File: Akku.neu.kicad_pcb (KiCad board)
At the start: 2 copper layers, 100 x 160 mm, 46 parts, among them P1 CONN_02X10, P2 CONN_02X10, P3 CONN_02X10, P4 CONN_01X01, P5 CONN_01X01, P6 CONN_01X01, SW1 SWITCH_INV, SW2 SWITCH_INV, SW3 SWITCH_INV, U1 7400, U2 7408, U3 4069, U4 74LS193, U5 74LS541, U6 74LS193, U7 74LS540, U8 74HC14

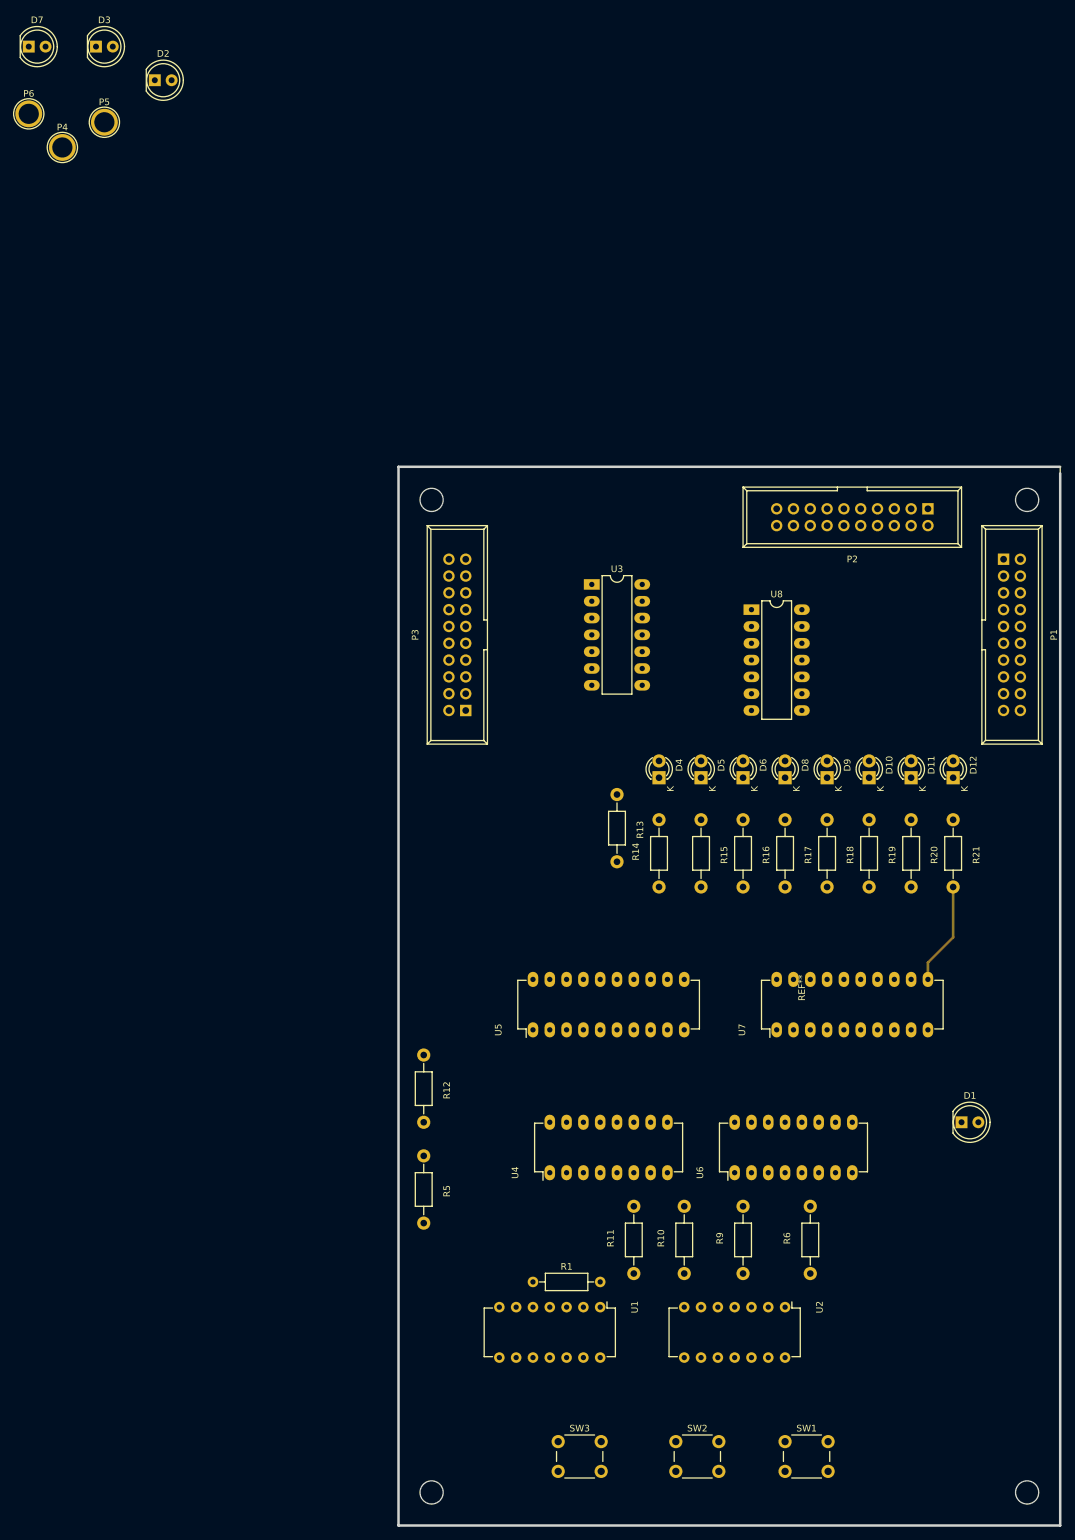
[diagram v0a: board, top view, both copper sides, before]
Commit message: Akku.sch fertiggestellt, Footprintfehler behoben, PCB Grundauslegung begonnen
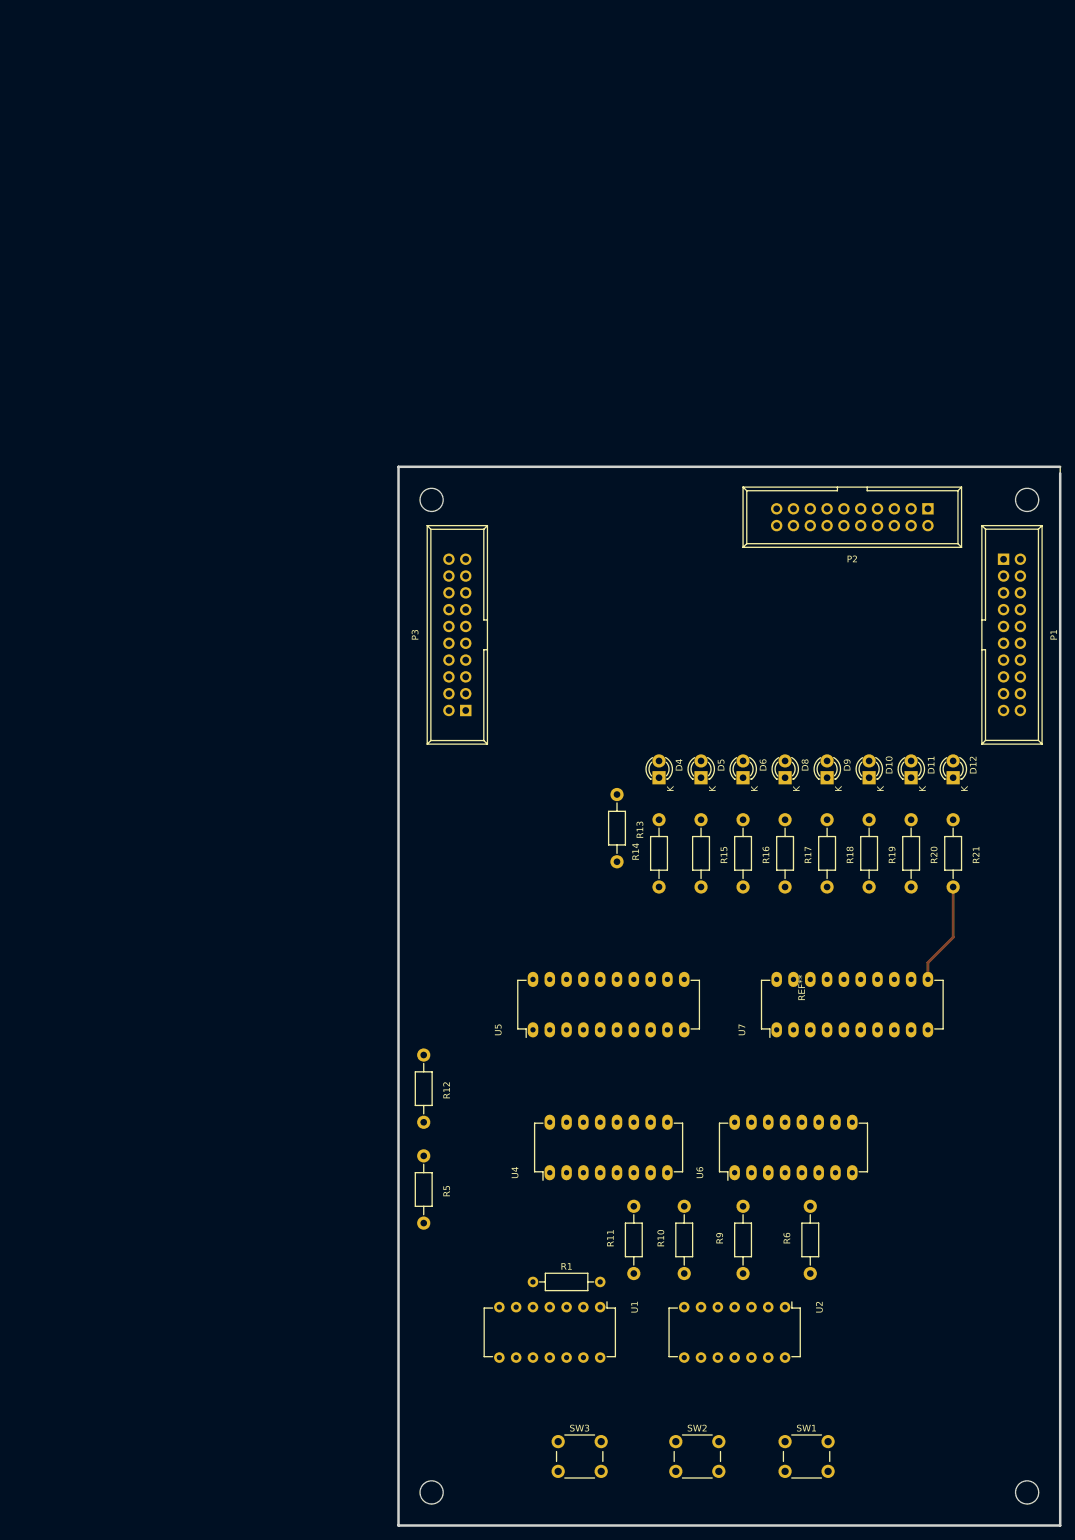
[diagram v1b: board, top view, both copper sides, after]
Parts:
- removed D1, D2, D3, D7: LED, LEDs:LED_D5.0mm_FlatTop
- removed P4, P5, P6: CONN_01X01, Connect:1pin
- removed U3: 4069, Housings_DIP:DIP-14_W7.62mm_LongPads
- removed U8: 74HC14, Housings_DIP:DIP-14_W7.62mm_LongPads

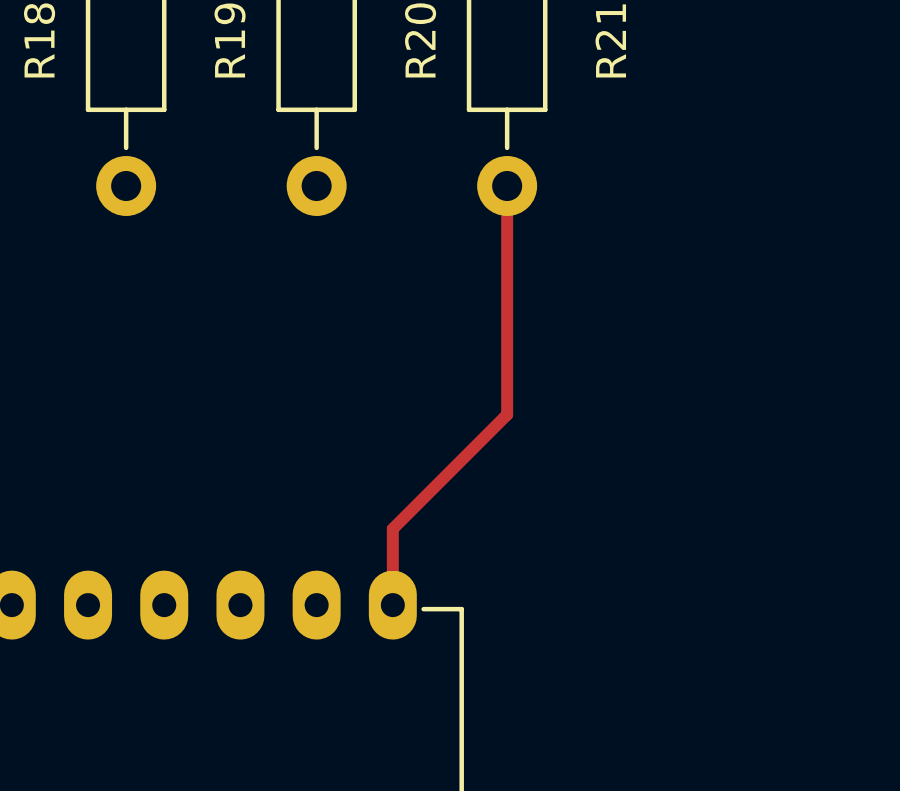
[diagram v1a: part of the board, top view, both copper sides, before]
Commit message: changed cupper front layer to bottom layer
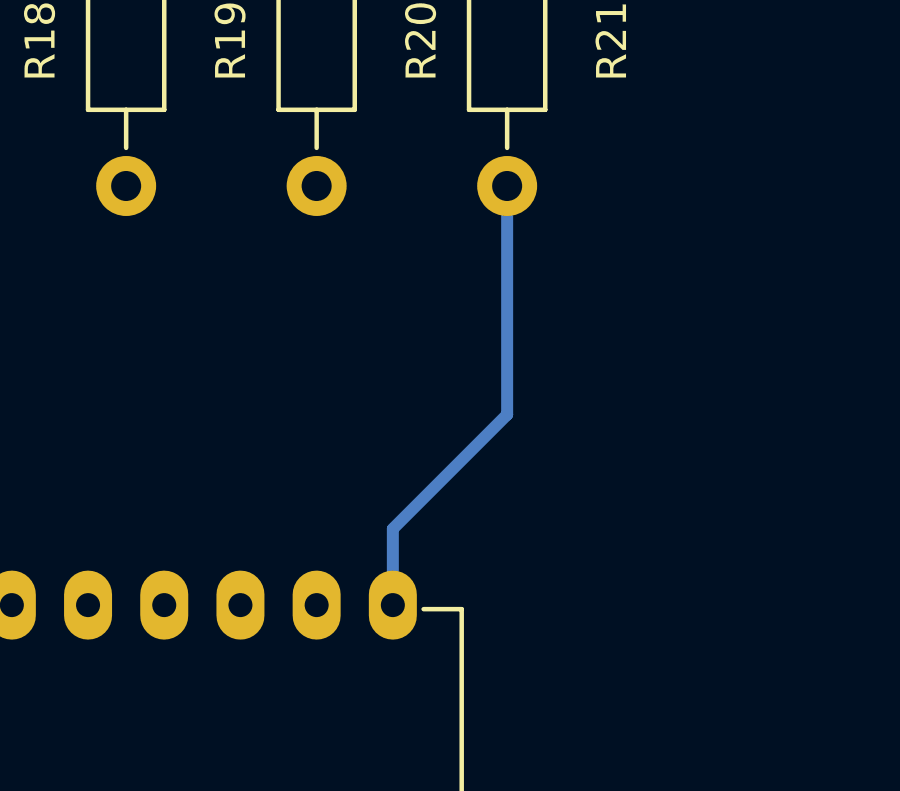
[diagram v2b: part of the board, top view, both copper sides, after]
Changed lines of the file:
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@@
-(kicad_pcb (version 4) (host pcbnew 4.0.4+e1-6308~48~ubuntu16.04.1-stable)
+(kicad_pcb (version 20171130) (host pcbnew 5.0.0-rc2-dev-unknown-0ded476~63~ubuntu16.04.1)
   (general
-    (links 143)
-    (no_connects 142)
-    (area 49.825 56.7 151.190301 217.540181)
     (thickness 1.6)
     (drawings 0)
@@
       (layerselection 0x00030_80000001)
       (usegerberextensions false)
+      (usegerberattributes false)
+      (usegerberadvancedattributes false)
+      (creategerberjobfile false)
       (excludeedgelayer true)
       (linewidth 0.100000)
@@
       (hpglpenspeed 20)
       (hpglpendiameter 15)
-      (hpglpenoverlay 2)
       (psnegative false)
       (psa4output false)
@@
       (net 2 VCC))
     (model LEDs.3dshapes/LED-3MM.wrl
-      (at (xyz 0.05 0 0))
+      (offset (xyz 1.269999980926514 0 0))
       (scale (xyz 1 1 1))
       (rotate (xyz 0 0 90))
@@
       (net 2 VCC))
     (model LEDs.3dshapes/LED-3MM.wrl
-      (at (xyz 0.05 0 0))
+      (offset (xyz 1.269999980926514 0 0))
       (scale (xyz 1 1 1))
       (rotate (xyz 0 0 90))
@@
       (net 2 VCC))
     (model LEDs.3dshapes/LED-3MM.wrl
-      (at (xyz 0.05 0 0))
+      (offset (xyz 1.269999980926514 0 0))
       (scale (xyz 1 1 1))
       (rotate (xyz 0 0 90))
@@
       (net 2 VCC))
     (model LEDs.3dshapes/LED-3MM.wrl
-      (at (xyz 0.05 0 0))
+      (offset (xyz 1.269999980926514 0 0))
       (scale (xyz 1 1 1))
       (rotate (xyz 0 0 90))
@@
       (net 2 VCC))
     (model LEDs.3dshapes/LED-3MM.wrl
-      (at (xyz 0.05 0 0))
+      (offset (xyz 1.269999980926514 0 0))
       (scale (xyz 1 1 1))
       (rotate (xyz 0 0 90))
@@
       (net 2 VCC))
     (model LEDs.3dshapes/LED-3MM.wrl
-      (at (xyz 0.05 0 0))
+      (offset (xyz 1.269999980926514 0 0))
       (scale (xyz 1 1 1))
       (rotate (xyz 0 0 90))
@@
       (net 2 VCC))
     (model LEDs.3dshapes/LED-3MM.wrl
-      (at (xyz 0.05 0 0))
+      (offset (xyz 1.269999980926514 0 0))
       (scale (xyz 1 1 1))
       (rotate (xyz 0 0 90))
@@
       (net 2 VCC))
     (model LEDs.3dshapes/LED-3MM.wrl
-      (at (xyz 0.05 0 0))
+      (offset (xyz 1.269999980926514 0 0))
       (scale (xyz 1 1 1))
       (rotate (xyz 0 0 90))
@@
       (net 20 up))
     (model Resistors_ThroughHole.3dshapes/Resistor_Horizontal_RM10mm.wrl
-      (at (xyz 0.2 0 0))
+      (offset (xyz 5.079999923706055 0 0))
       (scale (xyz 0.4 0.4 0.4))
       (rotate (xyz 0 0 0))
@@
       (net 21 down))
     (model Resistors_ThroughHole.3dshapes/Resistor_Horizontal_RM10mm.wrl
-      (at (xyz 0.2 0 0))
+      (offset (xyz 5.079999923706055 0 0))
       (scale (xyz 0.4 0.4 0.4))
       (rotate (xyz 0 0 0))
@@
       (net 23 GND))
     (model Resistors_ThroughHole.3dshapes/Resistor_Horizontal_RM10mm.wrl
-      (at (xyz 0.2 0 0))
+      (offset (xyz 5.079999923706055 0 0))
       (scale (xyz 0.4 0.4 0.4))
       (rotate (xyz 0 0 0))
@@
       (net 25 "Net-(D1-Pad2)"))
     (model Resistors_ThroughHole.3dshapes/Resistor_Horizontal_RM10mm.wrl
-      (at (xyz 0.2 0 0))
+      (offset (xyz 5.079999923706055 0 0))
       (scale (xyz 0.4 0.4 0.4))
       (rotate (xyz 0 0 0))
@@
       (net 27 "Net-(D2-Pad2)"))
     (model Resistors_ThroughHole.3dshapes/Resistor_Horizontal_RM10mm.wrl
-      (at (xyz 0.2 0 0))
+      (offset (xyz 5.079999923706055 0 0))
       (scale (xyz 0.4 0.4 0.4))
       (rotate (xyz 0 0 0))
@@
       (net 29 "Net-(R12-Pad2)"))
     (model Resistors_ThroughHole.3dshapes/Resistor_Horizontal_RM10mm.wrl
-      (at (xyz 0.2 0 0))
+      (offset (xyz 5.079999923706055 0 0))
       (scale (xyz 0.4 0.4 0.4))
       (rotate (xyz 0 0 0))
@@
       (net 30 "Net-(R13-Pad2)"))
     (model Resistors_ThroughHole.3dshapes/Resistor_Horizontal_RM10mm.wrl
-      (at (xyz 0.2 0 0))
+      (offset (xyz 5.079999923706055 0 0))
       (scale (xyz 0.4 0.4 0.4))
       (rotate (xyz 0 0 0))
@@
       (net 32 "Net-(D7-Pad2)"))
     (model Resistors_ThroughHole.3dshapes/Resistor_Horizontal_RM10mm.wrl
-      (at (xyz 0.2 0 0))
+      (offset (xyz 5.079999923706055 0 0))
       (scale (xyz 0.4 0.4 0.4))
       (rotate (xyz 0 0 0))
@@
       (net 33 "Net-(R15-Pad2)"))
     (model Resistors_ThroughHole.3dshapes/Resistor_Horizontal_RM10mm.wrl
-      (at (xyz 0.2 0 0))
+      (offset (xyz 5.079999923706055 0 0))
       (scale (xyz 0.4 0.4 0.4))
       (rotate (xyz 0 0 0))
@@
       (net 34 "Net-(R16-Pad2)"))
     (model Resistors_ThroughHole.3dshapes/Resistor_Horizontal_RM10mm.wrl
-      (at (xyz 0.2 0 0))
+      (offset (xyz 5.079999923706055 0 0))
       (scale (xyz 0.4 0.4 0.4))
       (rotate (xyz 0 0 0))
@@
       (net 35 "Net-(R17-Pad2)"))
     (model Resistors_ThroughHole.3dshapes/Resistor_Horizontal_RM10mm.wrl
-      (at (xyz 0.2 0 0))
+      (offset (xyz 5.079999923706055 0 0))
       (scale (xyz 0.4 0.4 0.4))
       (rotate (xyz 0 0 0))
@@
       (net 36 "Net-(R18-Pad2)"))
     (model Resistors_ThroughHole.3dshapes/Resistor_Horizontal_RM10mm.wrl
-      (at (xyz 0.2 0 0))
+      (offset (xyz 5.079999923706055 0 0))
       (scale (xyz 0.4 0.4 0.4))
       (rotate (xyz 0 0 0))
@@
       (net 37 "Net-(R19-Pad2)"))
     (model Resistors_ThroughHole.3dshapes/Resistor_Horizontal_RM10mm.wrl
-      (at (xyz 0.2 0 0))
+      (offset (xyz 5.079999923706055 0 0))
       (scale (xyz 0.4 0.4 0.4))
       (rotate (xyz 0 0 0))
@@
       (net 38 "Net-(R20-Pad2)"))
     (model Resistors_ThroughHole.3dshapes/Resistor_Horizontal_RM10mm.wrl
-      (at (xyz 0.2 0 0))
+      (offset (xyz 5.079999923706055 0 0))
       (scale (xyz 0.4 0.4 0.4))
       (rotate (xyz 0 0 0))
@@
       (net 39 "Net-(R21-Pad2)"))
     (model Resistors_ThroughHole.3dshapes/Resistor_Horizontal_RM10mm.wrl
-      (at (xyz 0.2 0 0))
+      (offset (xyz 5.079999923706055 0 0))
       (scale (xyz 0.4 0.4 0.4))
       (rotate (xyz 0 0 0))
@@
       (net 40 "Net-(R1-Pad2)"))
     (model Buttons_Switches_ThroughHole.3dshapes/SW_PUSH_6mm_h5mm.wrl
-      (at (xyz 0.005 0 0))
+      (offset (xyz 0.1269999980926514 0 0))
       (scale (xyz 0.3937 0.3937 0.3937))
       (rotate (xyz 0 0 0))
@@
       (net 41 "Net-(R4-Pad2)"))
     (model Buttons_Switches_ThroughHole.3dshapes/SW_PUSH_6mm_h5mm.wrl
-      (at (xyz 0.005 0 0))
+      (offset (xyz 0.1269999980926514 0 0))
       (scale (xyz 0.3937 0.3937 0.3937))
       (rotate (xyz 0 0 0))
@@
       (net 23 GND))
     (model Buttons_Switches_ThroughHole.3dshapes/SW_PUSH_6mm_h5mm.wrl
-      (at (xyz 0.005 0 0))
+      (offset (xyz 0.1269999980926514 0 0))
       (scale (xyz 0.3937 0.3937 0.3937))
       (rotate (xyz 0 0 0))
@@
     )
   )
-  (segment (start 130.81 134.62) (end 130.81 132.08) (width 0.4) (layer F.Cu) (net 39))
-  (segment (start 134.62 128.27) (end 134.62 120.65) (width 0.4) (layer F.Cu) (net 39))
-  (segment (start 130.81 132.08) (end 134.62 128.27) (width 0.4) (layer F.Cu) (net 39))
+  (segment (start 130.81 134.62) (end 130.81 132.08) (width 0.4) (layer B.Cu) (net 39))
+  (segment (start 134.62 128.27) (end 134.62 120.65) (width 0.4) (layer B.Cu) (net 39))
+  (segment (start 130.81 132.08) (end 134.62 128.27) (width 0.4) (layer B.Cu) (net 39))
 )
